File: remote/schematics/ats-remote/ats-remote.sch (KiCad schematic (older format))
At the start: 9 parts, among them J1 Conn_01x08, J2 Conn_01x08, J3 Conn_01x07, J4 Conn_01x07, J5 Conn_01x09, J6 Conn_01x09, U1 RFM95W-915S2, U2 PIC18F06Q40, U3 YIC71009EBGG

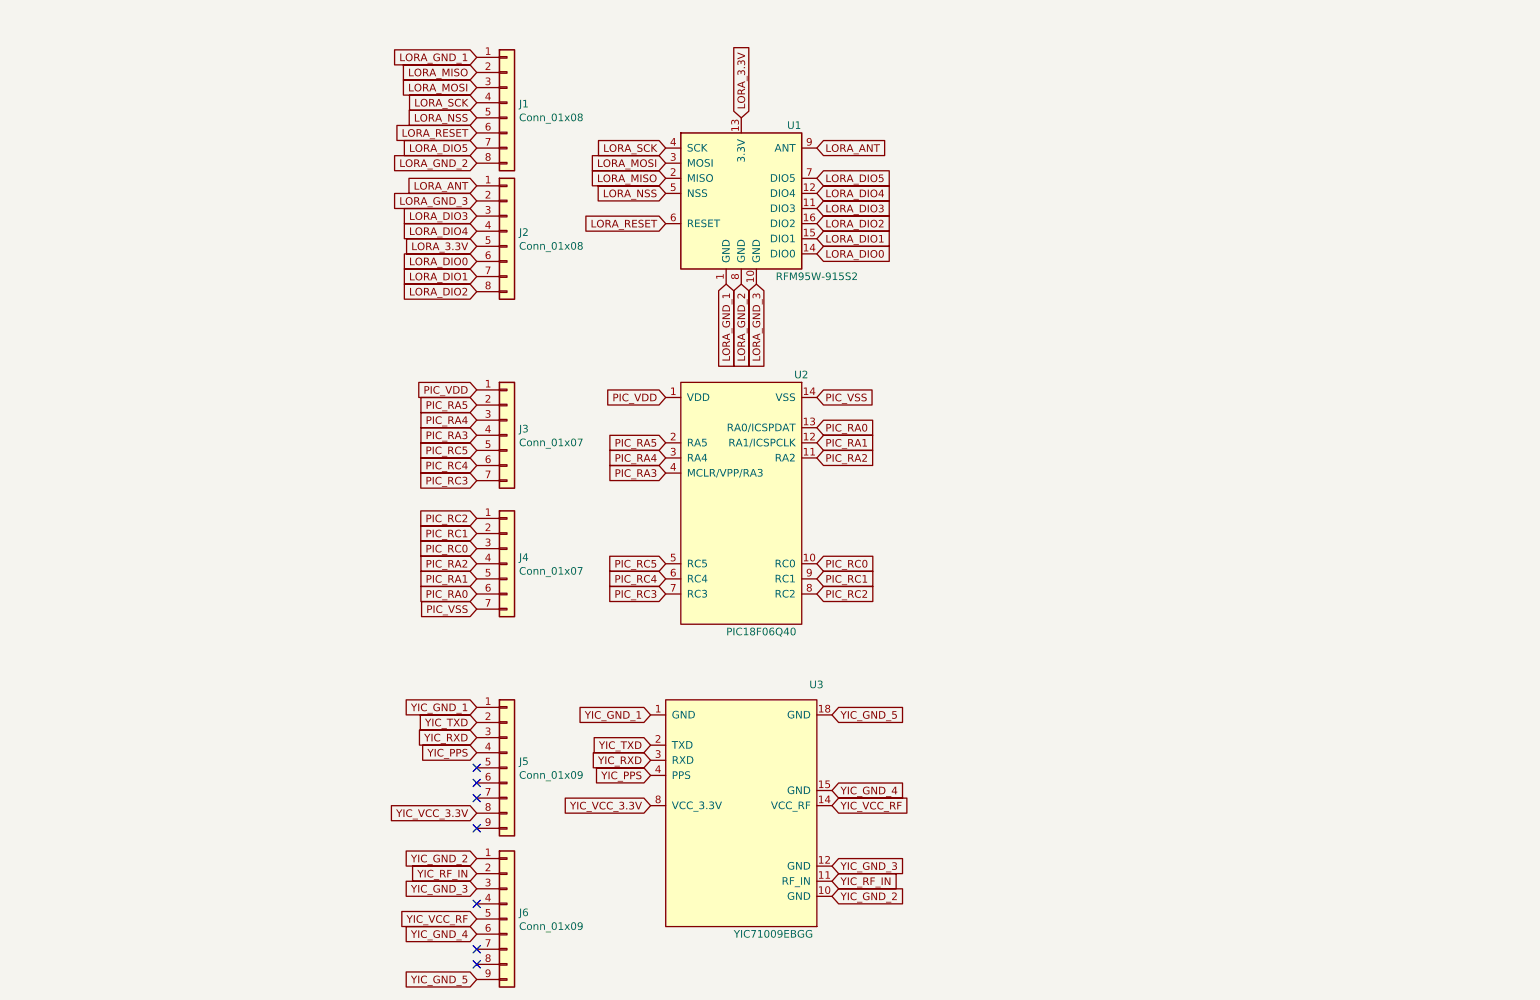
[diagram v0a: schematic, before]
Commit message: update schematic and pcb to v0.2.0
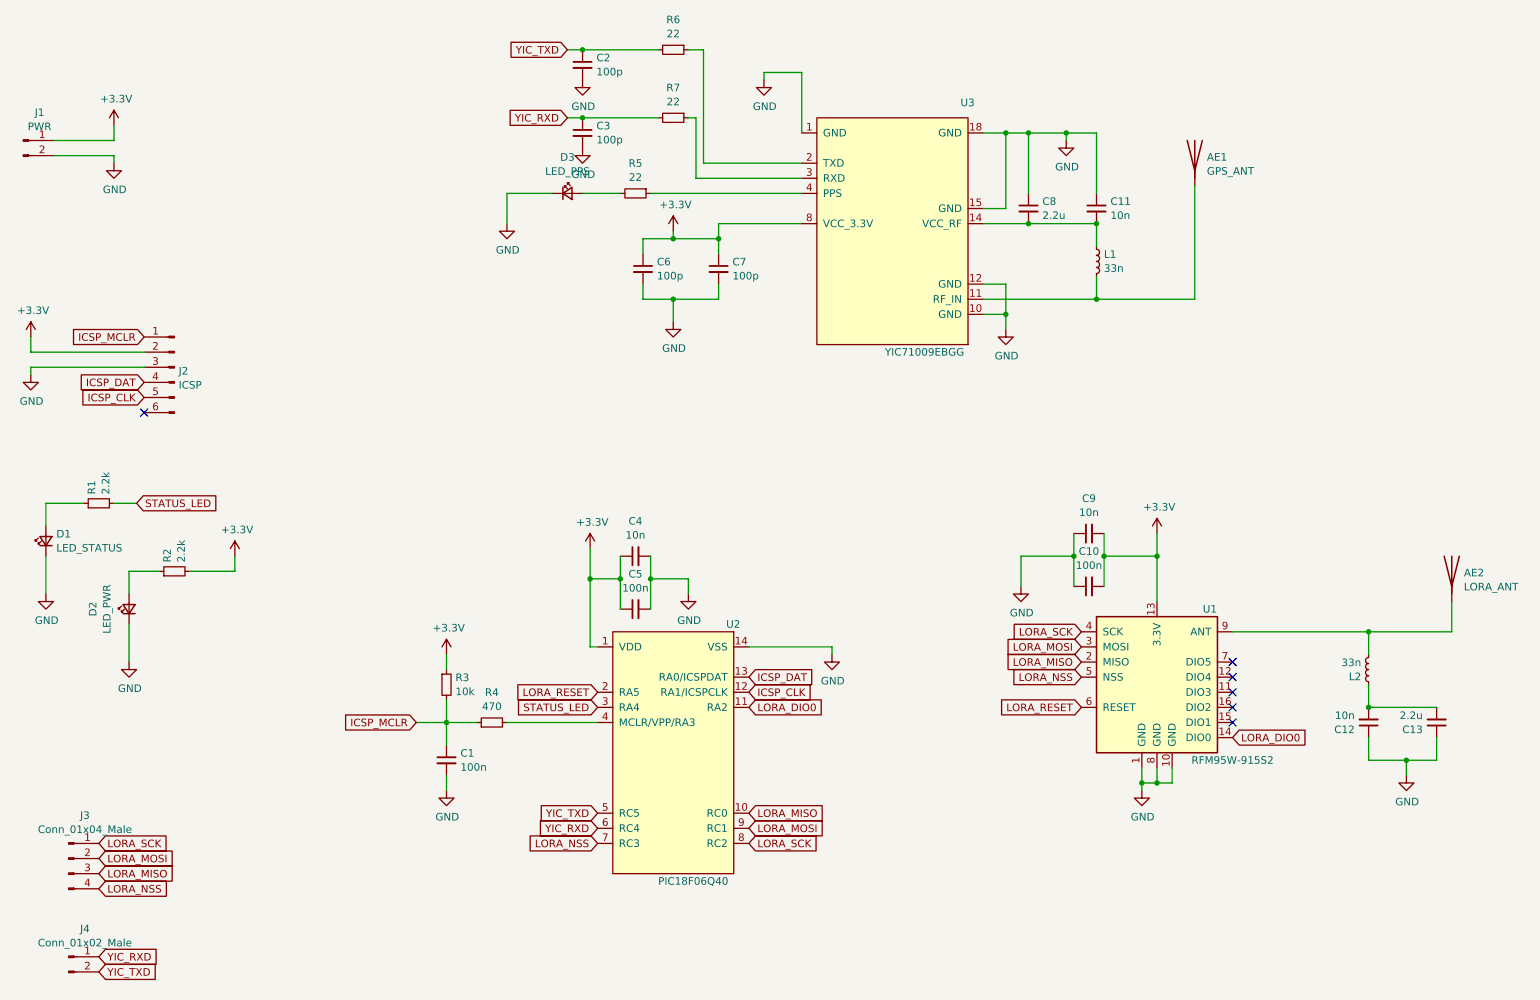
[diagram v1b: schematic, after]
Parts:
- removed J1, J2: Conn_01x08, Connector_PinSocket_1.27mm:PinSocket_1x08_P1.27mm_Vertical, symbol Connector_Generic:Conn_01x08
- removed J3, J4: Conn_01x07, Connector_PinSocket_1.27mm:PinSocket_1x07_P1.27mm_Vertical, symbol Connector_Generic:Conn_01x07
- removed J5, J6: Conn_01x09, Connector_PinSocket_1.27mm:PinSocket_1x09_P1.27mm_Vertical, symbol Connector_Generic:Conn_01x09
- added AE1: GPS_ANT, ats-remote:GPS_ANT_SR4G008, symbol Device:Antenna
- added AE2: LORA_ANT, ats-remote:LORA_ANT_YIC71009EBGG, symbol Device:Antenna
- added C1, C10, C5: 100n, Capacitor_SMD:C_0805_2012Metric_Pad1.18x1.45mm_HandSolder, symbol Device:C_Small
- added C11, C12, C4, C9: 10n, Capacitor_SMD:C_0805_2012Metric_Pad1.18x1.45mm_HandSolder, symbol Device:C_Small
- added C13, C8: 2.2u, Capacitor_SMD:C_0805_2012Metric_Pad1.18x1.45mm_HandSolder, symbol Device:C_Small
- added C2, C3, C6, C7: 100p, Capacitor_SMD:C_0805_2012Metric_Pad1.18x1.45mm_HandSolder, symbol Device:C_Small
- added D1: LED_STATUS, Diode_SMD:D_1206_3216Metric_Pad1.42x1.75mm_HandSolder, symbol Device:LED_Small
- added D2: LED_PWR, Diode_SMD:D_1206_3216Metric_Pad1.42x1.75mm_HandSolder, symbol Device:LED_Small
- added D3: LED_PPS, Diode_SMD:D_1206_3216Metric_Pad1.42x1.75mm_HandSolder, symbol Device:LED_Small
- added J1: PWR, Connector_PinHeader_1.27mm:PinHeader_1x02_P1.27mm_Vertical, symbol Connector:Conn_01x02_Male
- added J2: ICSP, Connector_PinHeader_1.27mm:PinHeader_1x06_P1.27mm_Vertical, symbol Connector:Conn_01x06_Male
- added J3: Conn_01x04_Male, Connector_PinHeader_1.27mm:PinHeader_1x04_P1.27mm_Vertical, symbol Connector:Conn_01x04_Male
- added J4: Conn_01x02_Male, Connector_PinHeader_1.27mm:PinHeader_1x02_P1.27mm_Vertical, symbol Connector:Conn_01x02_Male
- added L1, L2: 33n, Inductor_SMD:L_0603_1608Metric_Pad1.05x0.95mm_HandSolder, symbol Device:L_Small
- added R1, R2: 2.2k, Resistor_SMD:R_1206_3216Metric_Pad1.30x1.75mm_HandSolder, symbol Device:R_Small
- added R3: 10k, Resistor_SMD:R_1206_3216Metric_Pad1.30x1.75mm_HandSolder, symbol Device:R_Small
- added R4: 470, Resistor_SMD:R_1206_3216Metric_Pad1.30x1.75mm_HandSolder, symbol Device:R_Small
- added R5, R6, R7: 22, Resistor_SMD:R_1206_3216Metric_Pad1.30x1.75mm_HandSolder, symbol Device:R_Small
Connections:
- net LORA_GND_2 is gone; now on net GND: U1.8 (GND)
- net LORA_GND_3 is gone; now on net GND: U1.10 (GND)
- net PIC_RA2 is gone; now on net LORA_DIO0: U2.11 (RA2)
- net PIC_RA5 is gone; now on net LORA_RESET: U2.2 (RA5)
- net PIC_RC0 is gone; now on net LORA_MISO: U2.10 (RC0)
- net PIC_RC1 is gone; now on net LORA_MOSI: U2.9 (RC1)
- net PIC_RC2 is gone; now on net LORA_SCK: U2.8 (RC2)
- net PIC_RC3 is gone; now on net LORA_NSS: U2.7 (RC3)
- net PIC_RC4 is gone; now on net YIC_RXD: U2.6 (RC4)
- net PIC_RC5 is gone; now on net YIC_TXD: U2.5 (RC5)
- net PIC_VDD is gone; now on net +3V3: U2.1 (VDD)
- net PIC_VSS is gone; now on net GND: U2.14 (VSS)
- net YIC_GND_1 is gone; now on net GND: U3.1 (GND)
- net YIC_GND_2 is gone; now on net GND: U3.10 (GND)
- net YIC_GND_3 is gone; now on net GND: U3.12 (GND)
- net YIC_GND_4 is gone; now on net GND: U3.15 (GND)
- net YIC_GND_5 is gone; now on net GND: U3.18 (GND)
- net YIC_VCC_3.3V is gone; now on net +3V3: U3.8 (VCC_3.3V)
- net LORA_MISO: now also J3.3 (Pin_3)
- net LORA_MOSI: now also J3.2 (Pin_2)
- net LORA_NSS: now also J3.4 (Pin_4)
- net LORA_SCK: now also J3.1 (Pin_1)
- net YIC_RXD: now also C3.1, J4.1 (Pin_1), R7.2; no longer U3.3 (RXD)
- net YIC_TXD: now also C2.1, J4.2 (Pin_2), R6.2; no longer U3.2 (TXD)
- net LORA_3.3V renamed +3V3
- net +3V3: now also C10.2, C4.1, C5.1, C6.1, C7.1, C9.2, J1.1 (Pin_1), J2.2 (Pin_2), R2.2, R3.1
- net LORA_ANT: no longer names the net of U1.9 (ANT)
- net LORA_ANT: now also AE2.1 (A), L2.2
- net LORA_DIO1: no longer names the net of U1.15 (DIO1)
- net LORA_DIO2: no longer names the net of U1.16 (DIO2)
- net LORA_DIO3: no longer names the net of U1.11 (DIO3)
- net LORA_DIO4: no longer names the net of U1.12 (DIO4)
- net LORA_DIO5: no longer names the net of U1.7 (DIO5)
- net LORA_GND_1 renamed GND
- net GND: now also C1.2, C10.1, C11.1, C12.1, C13.1, C2.2, C3.2, C4.2, C5.2, C6.2, C7.2, C8.1, C9.1, D1.1 (K), D2.1 (K), D3.1 (K), J1.2 (Pin_2), J2.3 (Pin_3)
- net PIC_RA0 renamed ICSP_DAT
- net ICSP_DAT: now also J2.4 (Pin_4)
- net PIC_RA1 renamed ICSP_CLK
- net ICSP_CLK: now also J2.5 (Pin_5)
- net PIC_RA3: no longer names the net of U2.4 (MCLR/VPP/RA3)
- net PIC_RA3: now also R4.2
- net PIC_RA4 renamed STATUS_LED
- net STATUS_LED: now also R1.2
- net YIC_PPS: no longer names the net of U3.4 (PPS)
- net YIC_PPS: now also R5.1
- net YIC_RF_IN: no longer names the net of U3.11 (RF_IN)
- net YIC_RF_IN: now also AE1.1 (A), L1.2
- net YIC_VCC_RF: no longer names the net of U3.14 (VCC_RF)
- net YIC_VCC_RF: now also C11.2, C8.2, L1.1
- new net: R6.1, U3.2 (TXD)
- new net: R7.1, U3.3 (RXD)
- new net: D1.2 (A), R1.1
- new net: D2.2 (A), R2.1
- new net: D3.2 (A), R5.2
- new net: C12.2, C13.2, L2.1
- new net ICSP_MCLR: C1.1, J2.1 (Pin_1), R3.2, R4.1
- no-connect marks 7 -> 6
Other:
- moved on the sheet: U1, U2, U3

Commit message: update schematic and pcb
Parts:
- removed AE1: GPS_ANT, ats-remote:GPS_ANT_SR4G008, symbol Device:Antenna
- added AE1: GPS_ANT, ats-remote:GPS_ANT_SR4G008, symbol ats-remote:ACAG1204-915-T
- added C14: 10n, Capacitor_SMD:C_0805_2012Metric_Pad1.18x1.45mm_HandSolder, symbol Device:C_Small
- added L3, L4: 33n, Inductor_SMD:L_0603_1608Metric_Pad1.05x0.95mm_HandSolder, symbol Device:L_Small
- C13, C8: value 2.2u -> 2u2
- C6: value 100p -> 2u2
- C7: value 100p -> 10n
- J3: value Conn_01x04_Male -> SPI
- J4: value Conn_01x02_Male -> UART
- R1, R2: value 2.2k -> 2k2
- R5: value 22 -> 2k2
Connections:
- net GND: now also AE1.3 (GND), AE1.4 (GND), AE1.6 (GND), L3.2, L4.2
- net LORA_MISO: now also J3.2 (Pin_2); no longer J3.3 (Pin_3)
- net LORA_MOSI: now also J3.3 (Pin_3); no longer J3.2 (Pin_2)
- net LORA_NSS: now also J3.1 (Pin_1); no longer J3.4 (Pin_4)
- net LORA_SCK: now also J3.4 (Pin_4); no longer J3.1 (Pin_1)
- net at L1.2, U3.11 (RF_IN): now also C14.2, L3.1
- new net: AE1.2 (ANT), C14.1, L4.1
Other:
- moved on the sheet: D3
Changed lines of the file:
@@
 	10100 4750 10100 4550
-$Comp
-L Device:Antenna AE1
-U 1 1 61DAE6EE
-P 8400 1600
-F 0 "AE1" H 8480 1590 50  0000 L CNN
-F 1 "GPS_ANT" H 8480 1497 50  0000 L CNN
-F 2 "ats-remote:GPS_ANT_SR4G008" H 8400 1600 50  0001 C CNN
-F 3 "~" H 8400 1600 50  0001 C CNN
-	1    8400 1600
-	1    0    0    -1
-$EndComp
 $Comp
 L Device:LED_Small D1
@@
 P 1150 3900
 F 0 "R1" H 1209 3947 50  0000 L CNN
-F 1 "2.2k" H 1209 3854 50  0000 L CNN
+F 1 "2k2" H 1209 3854 50  0000 L CNN
 F 2 "Resistor_SMD:R_1206_3216Metric_Pad1.30x1.75mm_HandSolder" H 1150 3900 50  0001 C CNN
 F 3 "~" H 1150 3900 50  0001 C CNN
@@
 P 1650 4350
 F 0 "R2" H 1709 4397 50  0000 L CNN
-F 1 "2.2k" H 1709 4304 50  0000 L CNN
+F 1 "2k2" H 1709 4304 50  0000 L CNN
 F 2 "Resistor_SMD:R_1206_3216Metric_Pad1.30x1.75mm_HandSolder" H 1650 4350 50  0001 C CNN
 F 3 "~" H 1650 4350 50  0001 C CNN
@@
 P 7300 1950
 F 0 "C8" H 7392 1997 50  0000 L CNN
-F 1 "2.2u" H 7392 1904 50  0000 L CNN
+F 1 "2u2" H 7392 1904 50  0000 L CNN
 F 2 "Capacitor_SMD:C_0805_2012Metric_Pad1.18x1.45mm_HandSolder" H 7300 1950 50  0001 C CNN
 F 3 "~" H 7300 1950 50  0001 C CNN
@@
 Wire Wire Line
 	7750 1450 7750 1850
-Wire Wire Line
-	8400 1800 8400 2550
 Wire Wire Line
 	7000 2550 7750 2550
@@
 Wire Wire Line
 	7750 2400 7750 2550
-Connection ~ 7750 2550
-Wire Wire Line
-	7750 2550 8400 2550
 Wire Wire Line
 	5800 1750 5100 1750
@@
 P 4700 1850
 F 0 "R5" V 4501 1850 50  0000 C CNN
-F 1 "22" V 4594 1850 50  0000 C CNN
+F 1 "2k2" V 4594 1850 50  0000 C CNN
 F 2 "Resistor_SMD:R_1206_3216Metric_Pad1.30x1.75mm_HandSolder" H 4700 1850 50  0001 C CNN
 F 3 "~" H 4700 1850 50  0001 C CNN
@@
 L power:GND #PWR0120
 U 1 1 61F19544
-P 3850 2050
-F 0 "#PWR0120" H 3850 1800 50  0001 C CNN
-F 1 "GND" H 3855 1875 50  0000 C CNN
-F 2 "" H 3850 2050 50  0001 C CNN
-F 3 "" H 3850 2050 50  0001 C CNN
-	1    3850 2050
+P 3650 2050
+F 0 "#PWR0120" H 3650 1800 50  0001 C CNN
+F 1 "GND" H 3655 1875 50  0000 C CNN
+F 2 "" H 3650 2050 50  0001 C CNN
+F 3 "" H 3650 2050 50  0001 C CNN
+	1    3650 2050
 	1    0    0    -1
 $EndComp
@@
 L Device:LED_Small D3
 U 1 1 61F1DC27
-P 4250 1850
-F 0 "D3" H 4250 2089 50  0000 C CNN
-F 1 "LED_PPS" H 4250 1996 50  0000 C CNN
-F 2 "Diode_SMD:D_1206_3216Metric_Pad1.42x1.75mm_HandSolder" V 4250 1850 50  0001 C CNN
-F 3 "~" V 4250 1850 50  0001 C CNN
-	1    4250 1850
-	1    0    0    -1
-$EndComp
-Wire Wire Line
-	3850 1850 3850 2050
+P 4050 1850
+F 0 "D3" H 4050 2089 50  0000 C CNN
+F 1 "LED_PPS" H 4050 1996 50  0000 C CNN
+F 2 "Diode_SMD:D_1206_3216Metric_Pad1.42x1.75mm_HandSolder" V 4050 1850 50  0001 C CNN
+F 3 "~" V 4050 1850 50  0001 C CNN
+	1    4050 1850
+	1    0    0    -1
+$EndComp
+Wire Wire Line
+	3650 1850 3650 2050
 $Comp
 L Device:C_Small C3
@@
 P 4750 2350
 F 0 "C6" H 4842 2397 50  0000 L CNN
-F 1 "100p" H 4842 2304 50  0000 L CNN
+F 1 "2u2" H 4842 2304 50  0000 L CNN
 F 2 "Capacitor_SMD:C_0805_2012Metric_Pad1.18x1.45mm_HandSolder" H 4750 2350 50  0001 C CNN
 F 3 "~" H 4750 2350 50  0001 C CNN
@@
 P 5250 2350
 F 0 "C7" H 5342 2397 50  0000 L CNN
-F 1 "100p" H 5342 2304 50  0000 L CNN
+F 1 "10n" H 5342 2304 50  0000 L CNN
 F 2 "Capacitor_SMD:C_0805_2012Metric_Pad1.18x1.45mm_HandSolder" H 5250 2350 50  0001 C CNN
 F 3 "~" H 5250 2350 50  0001 C CNN
@@
 P 10000 5350
 F 0 "C13" H 10092 5397 50  0000 L CNN
-F 1 "2.2u" H 10092 5304 50  0000 L CNN
+F 1 "2u2" H 10092 5304 50  0000 L CNN
 F 2 "Capacitor_SMD:C_0805_2012Metric_Pad1.18x1.45mm_HandSolder" H 10000 5350 50  0001 C CNN
 F 3 "~" H 10000 5350 50  0001 C CNN
@@
 LORA_RESET
 Wire Wire Line
-	3850 1850 4150 1850
-Wire Wire Line
-	4350 1850 4600 1850
+	3650 1850 3950 1850
 Wire Wire Line
 	800  4050 800  3900
@@
 P 950 6250
 F 0 "J3" H 1058 6535 50  0000 C CNN
-F 1 "Conn_01x04_Male" H 1058 6442 50  0000 C CNN
+F 1 "SPI" H 1058 6442 50  0000 C CNN
 F 2 "Connector_PinHeader_1.27mm:PinHeader_1x04_P1.27mm_Vertical" H 950 6250 50  0001 C CNN
 F 3 "~" H 950 6250 50  0001 C CNN
@@
 P 950 6900
 F 0 "J4" H 1058 7085 50  0000 C CNN
-F 1 "Conn_01x02_Male" H 1058 6992 50  0000 C CNN
+F 1 "UART" H 1058 6992 50  0000 C CNN
 F 2 "Connector_PinHeader_1.27mm:PinHeader_1x02_P1.27mm_Vertical" H 950 6900 50  0001 C CNN
 F 3 "~" H 950 6900 50  0001 C CNN
@@
 	1    0    0    -1
 $EndComp
+Text GLabel 1150 6450 2    50   Input ~ 0
+LORA_SCK
+Text GLabel 1150 6350 2    50   Input ~ 0
+LORA_MOSI
+Text GLabel 1150 6250 2    50   Input ~ 0
+LORA_MISO
 Text GLabel 1150 6150 2    50   Input ~ 0
-LORA_SCK
-Text GLabel 1150 6250 2    50   Input ~ 0
-LORA_MOSI
-Text GLabel 1150 6350 2    50   Input ~ 0
-LORA_MISO
-Text GLabel 1150 6450 2    50   Input ~ 0
 LORA_NSS
 Text GLabel 1150 7000 2    50   Input ~ 0
@@
 Text GLabel 1150 6900 2    50   Input ~ 0
 YIC_RXD
+Wire Wire Line
+	4150 1850 4600 1850
+$Comp
+L Device:C_Small C14
+U 1 1 61CC5279
+P 8250 2550
+F 0 "C14" V 8021 2550 50  0000 C CNN
+F 1 "10n" V 8112 2550 50  0000 C CNN
+F 2 "Capacitor_SMD:C_0805_2012Metric_Pad1.18x1.45mm_HandSolder" H 8250 2550 50  0001 C CNN
+F 3 "~" H 8250 2550 50  0001 C CNN
+	1    8250 2550
+	0    1    1    0
+$EndComp
+$Comp
+L Device:L_Small L3
+U 1 1 61CC7ED4
+P 8000 2800
+F 0 "L3" H 8049 2847 50  0000 L CNN
+F 1 "33n" H 8049 2754 50  0000 L CNN
+F 2 "Inductor_SMD:L_0603_1608Metric_Pad1.05x0.95mm_HandSolder" H 8000 2800 50  0001 C CNN
+F 3 "~" H 8000 2800 50  0001 C CNN
+	1    8000 2800
+	1    0    0    -1
+$EndComp
+Wire Wire Line
+	8000 2900 8000 3050
+$Comp
+L Device:L_Small L4
+U 1 1 61CCBBC5
+P 8500 2800
+F 0 "L4" H 8549 2847 50  0000 L CNN
+F 1 "33n" H 8549 2754 50  0000 L CNN
+F 2 "Inductor_SMD:L_0603_1608Metric_Pad1.05x0.95mm_HandSolder" H 8500 2800 50  0001 C CNN
+F 3 "~" H 8500 2800 50  0001 C CNN
+	1    8500 2800
+	1    0    0    -1
+$EndComp
+Wire Wire Line
+	8500 2900 8500 3050
+Wire Wire Line
+	7750 2550 8000 2550
+Connection ~ 7750 2550
+Wire Wire Line
+	8000 2700 8000 2550
+Connection ~ 8000 2550
+Wire Wire Line
+	8000 2550 8150 2550
+$Comp
+L power:GND #PWR0125
+U 1 1 61CE9263
+P 8250 3100
+F 0 "#PWR0125" H 8250 2850 50  0001 C CNN
+F 1 "GND" H 8255 2925 50  0000 C CNN
+F 2 "" H 8250 3100 50  0001 C CNN
+F 3 "" H 8250 3100 50  0001 C CNN
+	1    8250 3100
+	1    0    0    -1
+$EndComp
+Wire Wire Line
+	8000 3050 8250 3050
+Wire Wire Line
+	8250 3050 8250 3100
+Wire Wire Line
+	8250 3050 8500 3050
+Connection ~ 8250 3050
+$Comp
+L ats-remote:ACAG1204-915-T AE1
+U 1 1 61D69634
+P 8950 1400
+F 0 "AE1" H 8500 1750 50  0000 L CNN
+F 1 "GPS_ANT" V 9500 1150 50  0000 L CNN
+F 2 "ats-remote:GPS_ANT_SR4G008" H 8950 2450 50  0001 C CNN
+F 3 "" H 8950 2450 50  0001 C CNN
+	1    8950 1400
+	1    0    0    -1
+$EndComp
+$Comp
+L power:GND #PWR0126
+U 1 1 61D7E716
+P 9400 1900
+F 0 "#PWR0126" H 9400 1650 50  0001 C CNN
+F 1 "GND" H 9405 1725 50  0000 C CNN
+F 2 "" H 9400 1900 50  0001 C CNN
+F 3 "" H 9400 1900 50  0001 C CNN
+	1    9400 1900
+	1    0    0    -1
+$EndComp
+Wire Wire Line
+	9200 1750 9200 1900
+Wire Wire Line
+	9200 1900 9300 1900
+Wire Wire Line
+	9300 1750 9300 1900
+Connection ~ 9300 1900
+Wire Wire Line
+	9300 1900 9400 1900
+Wire Wire Line
+	9400 1750 9400 1900
+Connection ~ 9400 1900
+Wire Wire Line
+	8350 2550 8500 2550
+Wire Wire Line
+	8500 2550 8500 1750
+Wire Wire Line
+	8500 2550 8500 2700
+Connection ~ 8500 2550
 $EndSCHEMATC
